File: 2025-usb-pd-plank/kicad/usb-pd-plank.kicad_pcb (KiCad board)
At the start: 2 copper layers, 41 x 35 mm, 37 parts, among them J1 USB_C_Receptacle_USB2.0_16P, J2 USB_C_Receptacle_USB2.0_16P, J3 Bus Pirate, J4 Bus Pirate, J5 LINK, Q1 AO3400A, Q2 AO3400A, Q3 AO3400A, Q4 AO3400A, U1 PTN5110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

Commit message: 2025-usb-pd-plank: placed and routed
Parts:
- removed U2, U3: NX20P5090, lib:WLCSP-15_3x5_B1.54_2.56mm_P0.5mm
- added Q5: AO4407A, lib:SO-8_3.9x4.9mm_P1.27mm, F.Cu at (62.8, 86.8)
- added Q6: AO4407A, lib:SO-8_3.9x4.9mm_P1.27mm, F.Cu at (70.2, 86.8)
- added Q7: AO4407A, lib:SO-8_3.9x4.9mm_P1.27mm, F.Cu at (70.2, 113.2)
- added Q8: AO4407A, lib:SO-8_3.9x4.9mm_P1.27mm, F.Cu at (62.8, 113.2)
- added R12: 100k, lib:R_0402_1005Metric, F.Cu at (62.8, 83.5)
- added R13: 10k, lib:R_0402_1005Metric, F.Cu at (71.5, 90.5)
- added R14: 10k, lib:R_0402_1005Metric, F.Cu at (69.0, 109.0)
- added R15: 100k, lib:R_0402_1005Metric, F.Cu at (70.2, 116.5)
- TP1, TP2: moved to B.Cu
- moved C6 15.1 mm to (45.8, 88.8), turned to -90 degrees
- moved C5 14.3 mm to (43.4, 88.8), turned to -90 degrees
- moved C3 8.73 mm to (65.0, 96.5), turned to 180 degrees
- moved R9 8.05 mm to (64.0, 108.2), turned to 90 degrees
- moved R7 6.80 mm to (60.7, 116.5)
- moved R8 6.77 mm to (66.5, 91.2), turned to 90 degrees
- moved TP2 5.69 mm to (62.1, 96.9), turned to 180 degrees
- moved Q1 5.58 mm to (69.0, 91.3), turned to 0 degrees
- moved R5 5.20 mm to (72.2, 83.5), turned to 0 degrees
- moved R10 5.01 mm to (60.2, 83.5), turned to 0 degrees
- moved Q3 4.81 mm to (64.0, 91.3)
- moved Q2 4.25 mm to (66.5, 108.2), turned to 0 degrees
- moved D1 4.03 mm to (43.5, 84.5), turned to -90 degrees
- moved Q4 3.88 mm to (61.5, 108.2)
- moved TP1 2.45 mm to (67.0, 100.1), turned to 180 degrees
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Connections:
- J3 pad 4: /~{ALERT} -> /EN_SRC
- J3 pad 6: /EN_SRC -> /~{ALERT}
- J4 pad 4: /~{ALERT} -> /EN_SRC
- J4 pad 6: /EN_SRC -> /~{ALERT}
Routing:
- net +5V: track 5.00 -> 106.2 mm, vias 0 -> 8
- net /USBIN_VBUS: track 2.00 -> 53.0 mm, vias 0 -> 4
- net /EN_SNK: track 0.00 -> 50.3 mm, vias 0 -> 6
- net /USBOUT_VBUS: track 27.8 -> 75.8 mm, vias 0 -> 2
- net /~{FAULT}: track 0.00 -> 46.4 mm, vias 0 -> 4
- net /USBIN_CC2: track 0.00 -> 46.2 mm, vias 0 -> 3
- net /I2C_SDA: track 0.00 -> 46.1 mm, vias 0 -> 6
- net /I2C_SCL: track 0.00 -> 45.7 mm, vias 0 -> 8
- net /EN_SRC: track 0.00 -> 43.8 mm, vias 0 -> 4
- net /~{ALERT}: track 0.00 -> 43.0 mm, vias 0 -> 2
- net /USBIN_CC1: track 0.00 -> 42.4 mm
- net /USBIN_SBU2: track 0.00 -> 21.2 mm, vias 0 -> 2
- net Net-(Q7-G): track 0.00 -> 18.9 mm, vias 0 -> 2
- net Net-(Q5-G): track 0.00 -> 16.1 mm, vias 0 -> 2
- net /USBIN_DB_P: track 0.00 -> 15.5 mm, vias 0 -> 2
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- added copper zone on B.Cu, net GND
- added copper zone on F.Cu, net GND
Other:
- board size 41 x 35 mm -> 41.2 x 35 mm

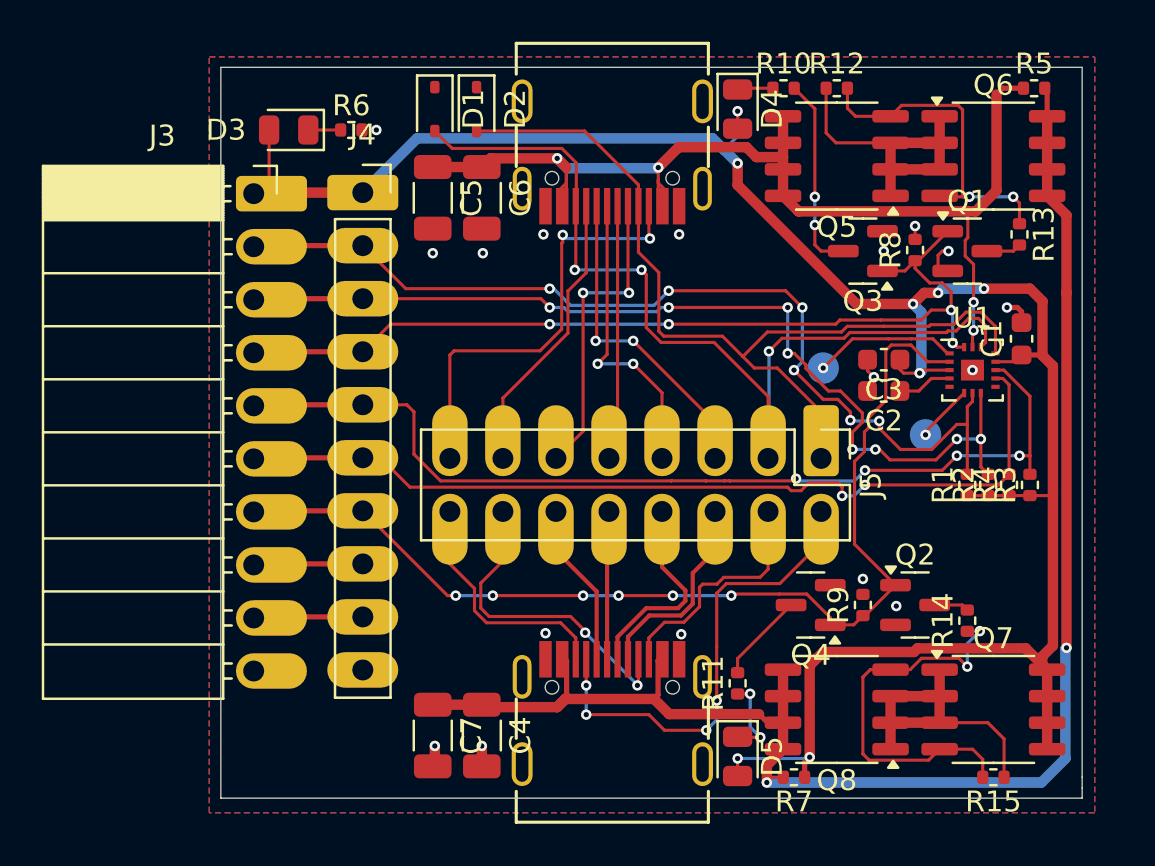
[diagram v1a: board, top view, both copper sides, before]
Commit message: 2025-usb-pd-plank: read for mfg
Changed i2c resistors to 10k
Changed all LEDs to green
Changed all power caps to 4.7uF/50V
(cost reduction by $us10)
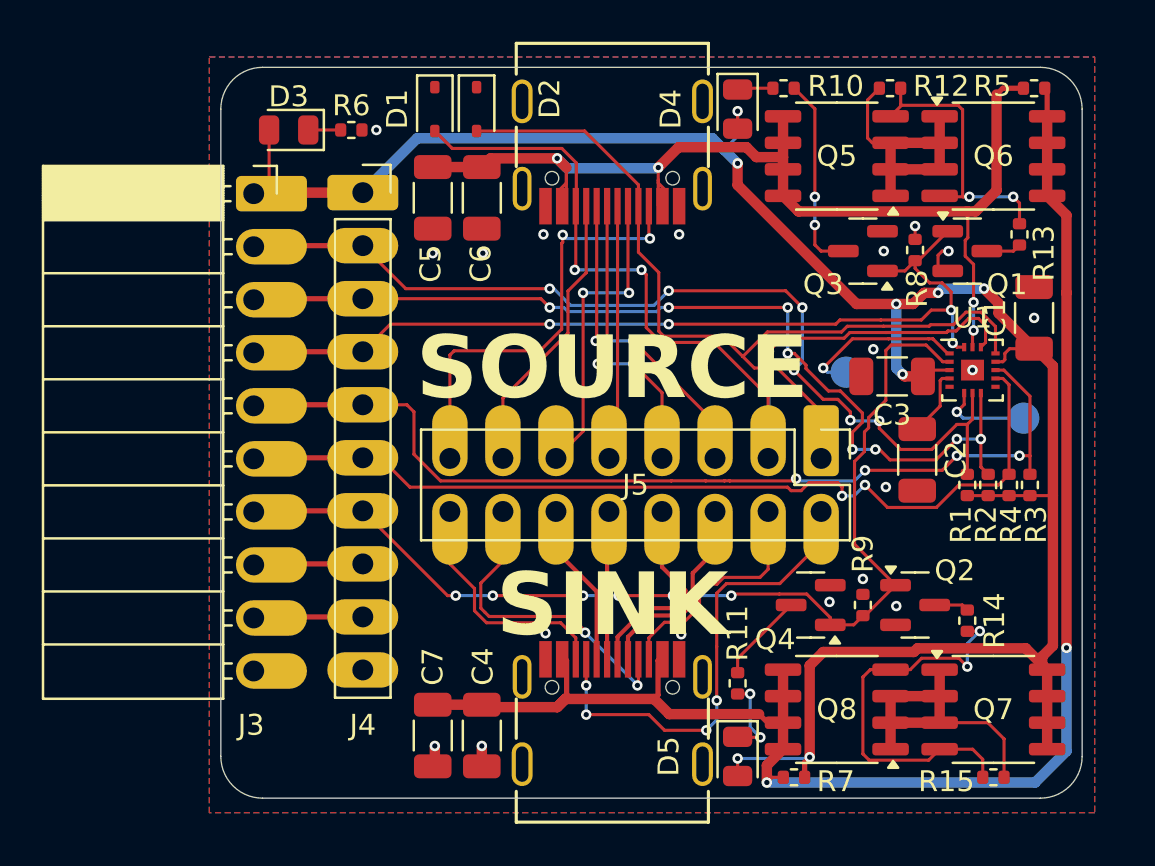
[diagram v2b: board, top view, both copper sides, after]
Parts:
- C1, C2, C3: value 2.2uF/16V -> 4.7uF/50V; footprint lib:C_0603_1608Metric -> lib:C_1206_3216Metric
- C5: value 1uF/50V -> 4.7uF/50V
- D3: value RED -> GREEN
- D5: value YELLOW -> GREEN
- R1, R2: value 4.7k -> 10k
- moved TP1 4.77 mm to (71.7, 99.3)
- moved C2 3.67 mm to (66.6, 101.3), turned to -90 degrees
- moved R12 2.55 mm to (65.3, 83.5)
- moved C1 1.17 mm to (72.2, 94.5)
- moved TP2 1.12 mm to (63.2, 97.1)
- moved C3 0.89 mm to (65.4, 97.3)
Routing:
- net GND: track 6.93 -> 3.87 mm, vias 17 -> 19
- net Net-(Q5-G): track 16.1 -> 13.7 mm
- net +5V: track 106.2 -> 104.2 mm
- net Net-(Q5-S-Pad1): track 15.2 -> 13.6 mm
- net Net-(U1-ILM_5_VBUS): track 2.77 -> 4.37 mm
- net Net-(U1-FRS_EN): track 6.92 -> 8.10 mm
- net /~{ALERT}: track 43.0 -> 43.9 mm
- net Net-(U1-BYPASS): track 2.62 -> 3.27 mm
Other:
- outline, holes or cut-outs redrawn
- board text added: "SINK"
- board text added: "SOURCE"
- board text added: "USB PD PLANK Apr2025 @TomKeddie"

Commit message: 2025-usb-pd-plank: add VBUS connector, silk fixes.  As submitted.
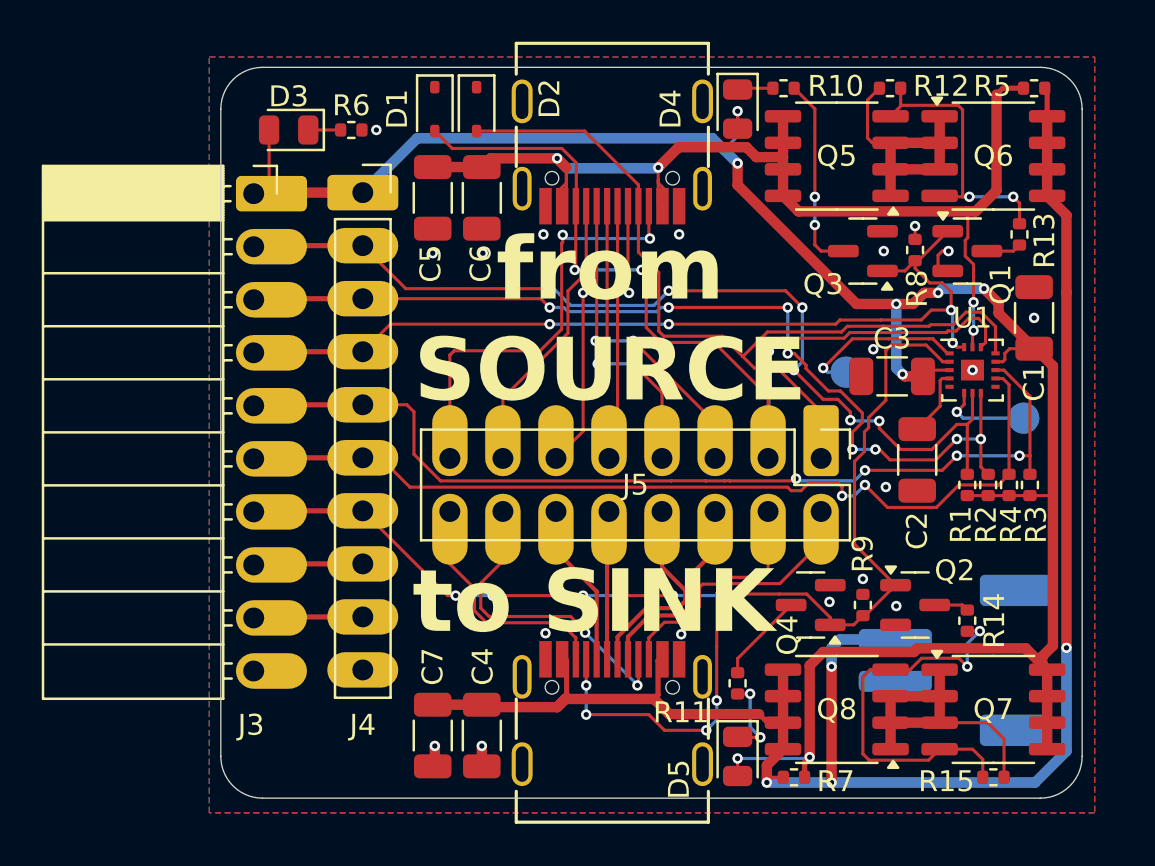
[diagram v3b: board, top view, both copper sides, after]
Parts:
- added J6: Conn_01x02, lib:JST_PH_S2B-PH-SM4-TB_1x02-1MP_P2.00mm_Horizontal, B.Cu at (68.4, 110.9)
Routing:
- net /USBOUT_VBUS: track 75.6 -> 85.3 mm, vias 2 -> 4
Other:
- board text added: "+"
- board text added: "from SOURCE"
- board text added: "to SINK"
- board text removed: "SINK"
- board text removed: "SOURCE"
